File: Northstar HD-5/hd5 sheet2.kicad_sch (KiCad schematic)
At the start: 69 parts, among them U1A 26LS32, U1C 74S10, U1D 74S00, U1F 74S04, U1H 74LS123, U2A 100ns_Delay, U2B 74LS161, U2C 74LS74, U2H 74LS283, U2J 74LS393, U3A 74S74, U3B 74S02, U3C 74LS161, U3D 74LS04, U3E 74LS161, U3F 74LS393, U3H 74LS273, U3J 74LS193, U4A 74S74, U4B 74S02, U4C 74S74, U4D 74S04, U4F 74LS193, U4H 74LS193, U4J 74LS04, U5D 74S124, U5F 74S74, U5H 74LS32, U5J 74LS00, U5K 74LS279

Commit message: changes to hd-5 and gitignore
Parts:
- C10, C11, C5: footprint (none) -> Capacitor_THT:C_Rect_L10.0mm_W5.0mm_P5.00mm_P7.50mm
- C14: footprint (none) -> Capacitor_THT:C_Disc_D10.0mm_W2.5mm_P5.00mm
- C17, C18, C19, C20: renamed from C?; footprint (none) -> Capacitor_THT:C_Disc_D10.0mm_W2.5mm_P5.00mm
- C6: renamed from C?; value 33nF 5% -> 33pF 1%; footprint (none) -> Capacitor_THT:C_Rect_L10.0mm_W5.0mm_P5.00mm_P7.50mm
- C8: footprint (none) -> Capacitor_THT:C_Rect_L7.0mm_W3.5mm_P2.50mm_P5.00mm
- CR1, CR2: footprint Diode_THT:D_DO-35_SOD27_P7.62mm_Horizontal -> Diode_THT:D_A-405_P12.70mm_Horizontal
- R10, R11, R15, R16, R17, R8: footprint (none) -> Resistor_THT:R_Axial_DIN0207_L6.3mm_D2.5mm_P15.24mm_Horizontal
- R12, R14, R18, R19, R20, R21, R22, R28, R7: footprint (none) -> Resistor_THT:R_Axial_DIN0309_L9.0mm_D3.2mm_P12.70mm_Horizontal
- R13: footprint (none) -> Potentiometer_THT:Potentiometer_Bourns_3009Y_Horizontal
- R29, R9: renamed from R?; footprint (none) -> Resistor_THT:R_Axial_DIN0207_L6.3mm_D2.5mm_P15.24mm_Horizontal
- TP1, TP10, TP11, TP12, TP13, TP3, TP4, TP6, TP9: footprint (none) -> Connector_PinHeader_2.54mm:PinHeader_1x01_P2.54mm_Vertical
- U1A1: renamed from U1A; footprint (none) -> Package_DIP:DIP-16_W7.62mm
- U1C1: renamed from U1C; footprint (none) -> Package_DIP:DIP-14_W7.62mm
- U1D1: renamed from U1D; footprint (none) -> Package_DIP:DIP-14_W7.62mm
- U1F1: renamed from U1F; footprint (none) -> Package_DIP:DIP-14_W7.62mm
- U1H1: renamed from U1H; footprint (none) -> Package_DIP:DIP-16_W7.62mm
- U2A1: renamed from U2A; footprint (none) -> Package_DIP:DIP-14_W7.62mm
- U2B1: renamed from U2B; footprint (none) -> Package_DIP:DIP-16_W7.62mm
- U2C1: renamed from U2C; footprint (none) -> Package_DIP:DIP-14_W7.62mm
- U2H1: renamed from U2H; footprint (none) -> Package_DIP:DIP-16_W7.62mm
- U2J1: renamed from U2J; footprint (none) -> Package_DIP:DIP-14_W7.62mm
- U3A1: renamed from U3A; footprint (none) -> Package_DIP:DIP-14_W7.62mm
- U3B1: renamed from U3B; footprint (none) -> Package_DIP:DIP-14_W7.62mm
- U3C1: renamed from U3C; footprint (none) -> Package_DIP:DIP-16_W7.62mm
- U3D1: renamed from U3D; footprint (none) -> Package_DIP:DIP-14_W7.62mm
- U3E1: renamed from U3E; footprint (none) -> Package_DIP:DIP-16_W7.62mm
- U3F1: renamed from U3F; footprint (none) -> Package_DIP:DIP-14_W7.62mm
- U3H1: renamed from U3H; footprint (none) -> Package_DIP:DIP-20_W7.62mm
- U3J1: renamed from U3J; footprint (none) -> Package_DIP:DIP-16_W7.62mm
- U4A1: renamed from U4A; footprint (none) -> Package_DIP:DIP-14_W7.62mm
- U4B1: renamed from U4B; footprint (none) -> Package_DIP:DIP-14_W7.62mm
- U4C1: renamed from U4C; footprint (none) -> Package_DIP:DIP-14_W7.62mm
- U4D1: renamed from U4D; footprint (none) -> Package_DIP:DIP-14_W7.62mm
- U4F1: renamed from U4F; footprint (none) -> Package_DIP:DIP-16_W7.62mm
- U4H1: renamed from U4H; footprint (none) -> Package_DIP:DIP-16_W7.62mm
- U4J1: renamed from U4J; footprint (none) -> Package_DIP:DIP-14_W7.62mm
- U5D1: renamed from U5D; footprint (none) -> Package_DIP:DIP-16_W7.62mm
- U5F1: renamed from U5F; footprint (none) -> Package_DIP:DIP-14_W7.62mm
- U5H1: renamed from U5H; footprint (none) -> Package_DIP:DIP-14_W7.62mm
- U5J1: renamed from U5J; footprint (none) -> Package_DIP:DIP-14_W7.62mm
- U5K1: renamed from U5K; footprint (none) -> Package_DIP:DIP-16_W7.62mm

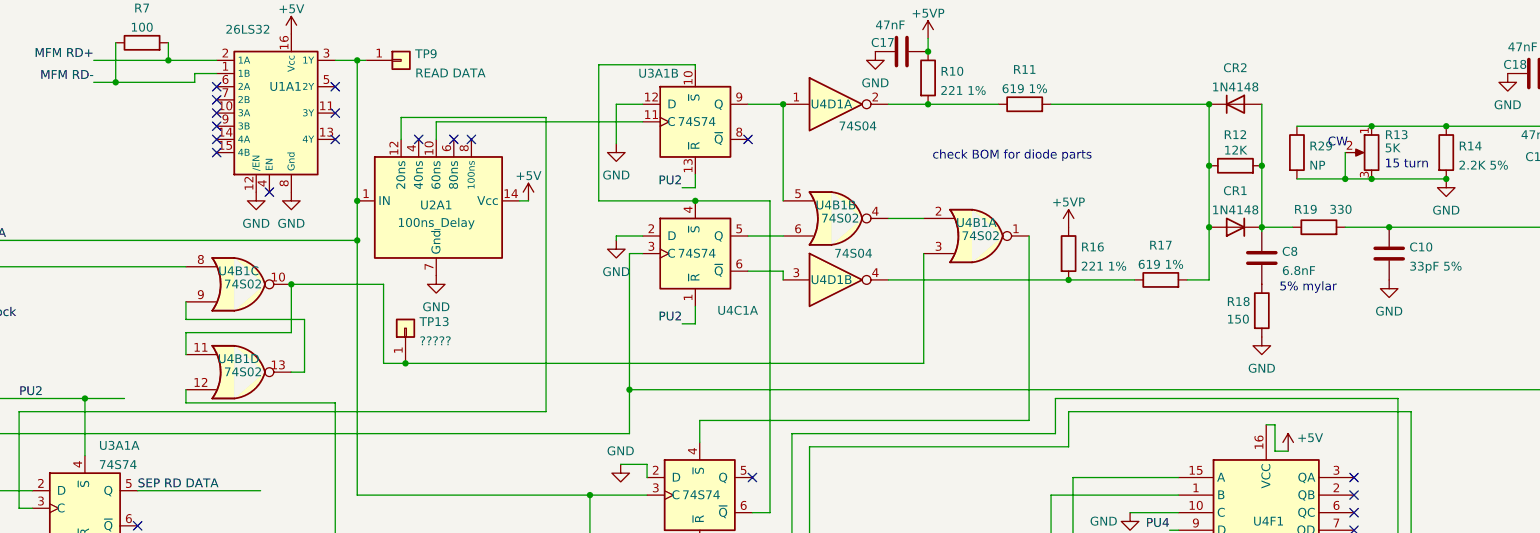
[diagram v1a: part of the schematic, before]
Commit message: placed components for column 5
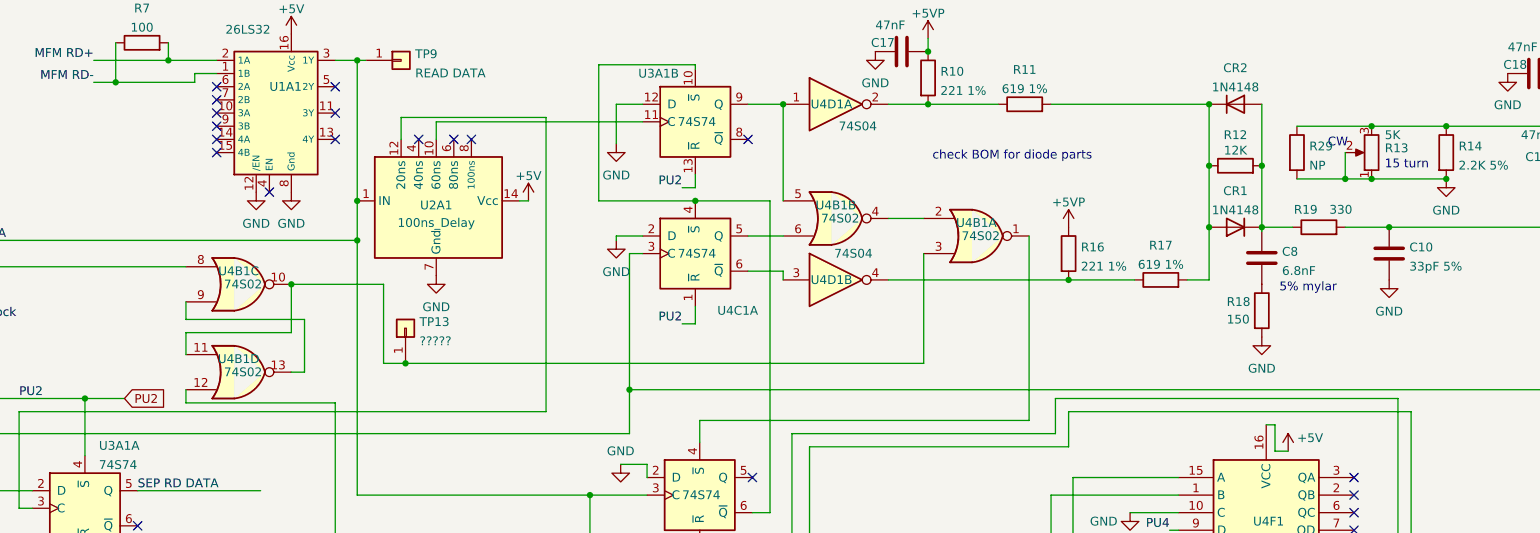
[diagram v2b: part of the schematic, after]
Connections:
- net GND: now also R13.1; no longer R13.3
- net at C19.1, R14.1, R15.2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: now also R13.3; no longer R13.1
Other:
- moved on the sheet: R13
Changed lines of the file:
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@@
     (effects (font (size 1.27 1.27)) (justify left bottom))
+  )
+  (global_label "PU2" (shape input) (at 103.505 127.635 0) (fields_autoplaced)
+    (effects (font (size 1.27 1.27)) (justify left))
+    (property "Intersheet References" "${INTERSHEET_REFS}" (id 0) (at 109.7281 127.5556 0)
+      (effects (font (size 1.27 1.27)) (justify left) hide)
+    )
   )
   (symbol (lib_id "Device:C") (at 307.34 80.645 270) (unit 1)
@@
     (pin "1")
   )
-  (symbol (lib_id "Device:R_Potentiometer") (at 283.845 92.075 0) (mirror y) (unit 1)
-    (in_bom yes) (on_board yes)
-    (property "Reference" "R13" (id 0) (at 285.75 89.535 0)
+  (symbol (lib_id "Device:R_Potentiometer") (at 283.845 92.075 180) (unit 1)
+    (in_bom yes) (on_board yes)
+    (property "Reference" "R13" (id 0) (at 285.75 91.44 0)
       (effects (font (size 1.27 1.27)) (justify right))
     )
-    (property "Value" "5K" (id 1) (at 285.75 91.44 0)
+    (property "Value" "5K" (id 1) (at 285.75 89.535 0)
       (effects (font (size 1.27 1.27)) (justify right))
     )

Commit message: placed components and repaired multi sheet labels
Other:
- moved on the sheet: U1C1C, U1F1D, U3B1A, U3B1D, U3D1E, U4J1A, U5J1B
